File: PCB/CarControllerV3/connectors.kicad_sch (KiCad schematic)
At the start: 44 parts, among them J1 649012227222, J2 649012227222, Q2 AO3400A, U13 PC817X1NIP1B, U21 AP74700QW6-7

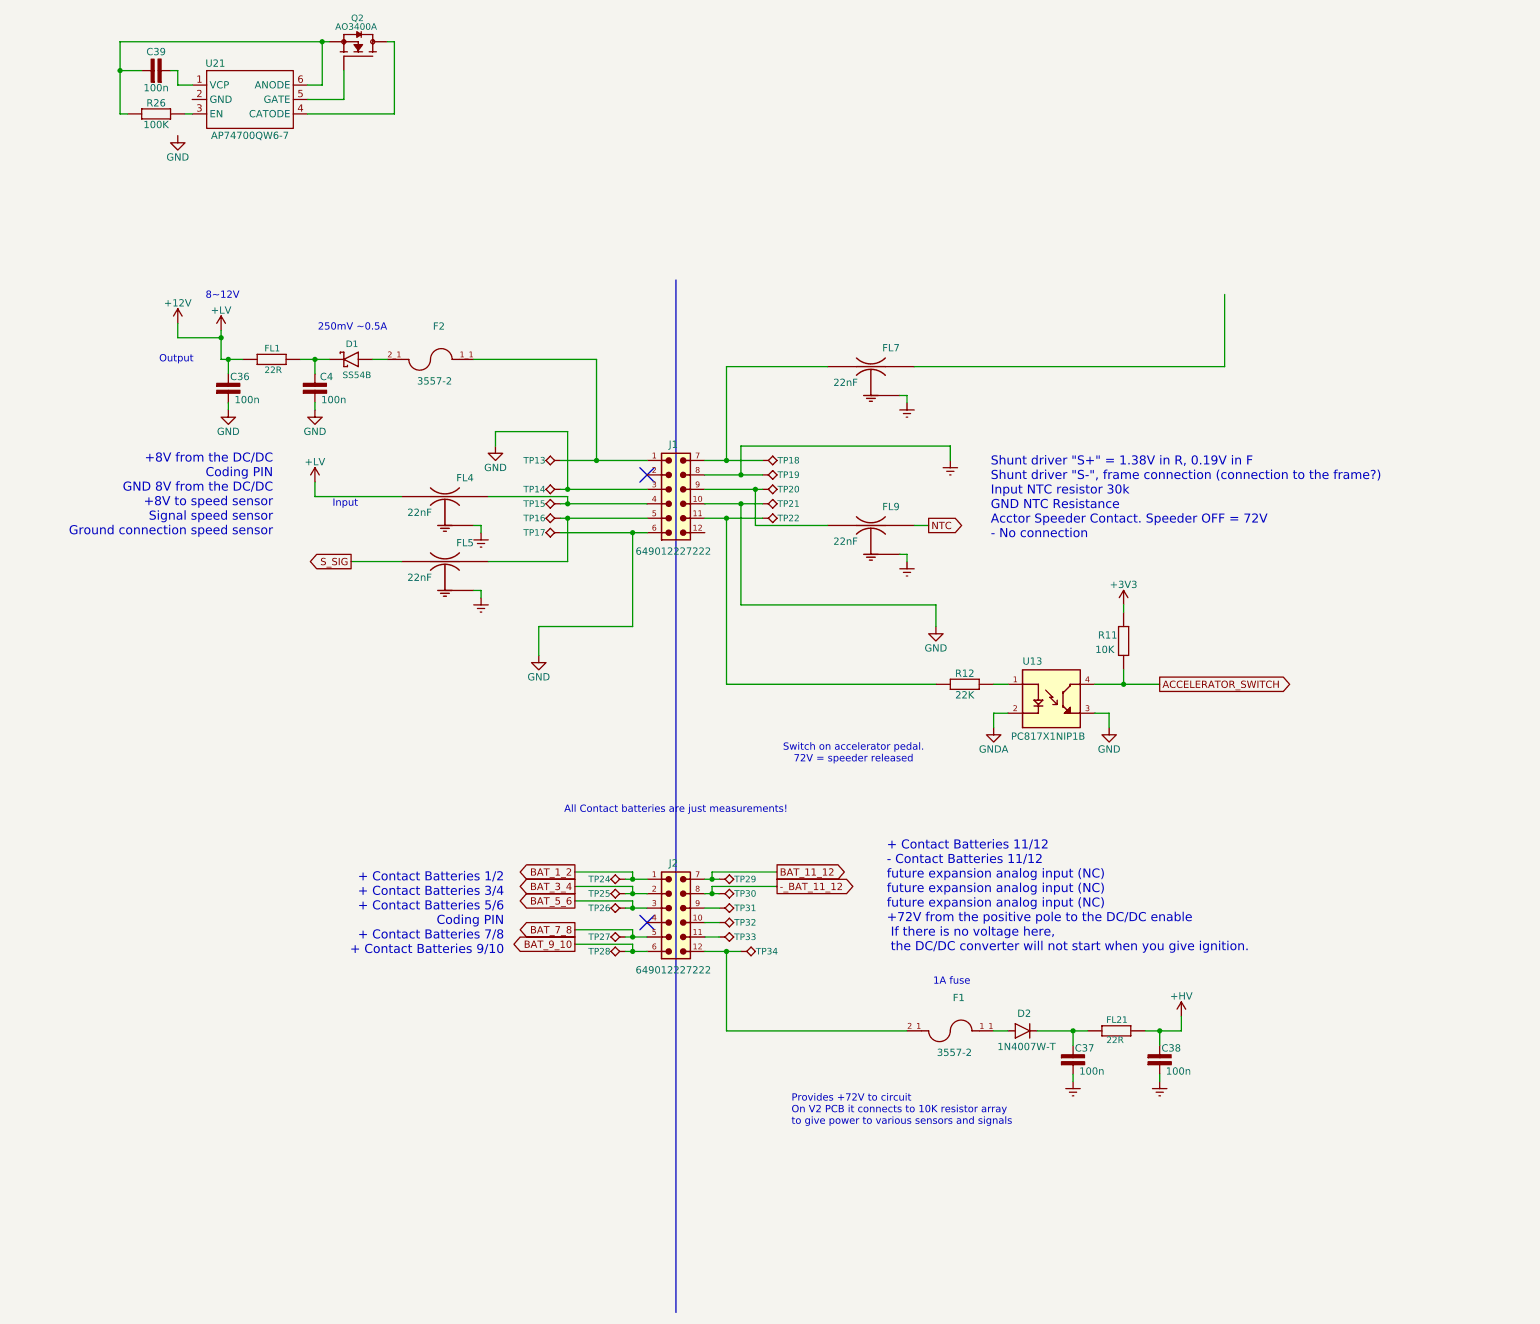
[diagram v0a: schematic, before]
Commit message: More work to PCB
- Rerouted bunch of connections
- Added alternative charge pump circuit
- Bunch of work on analog circuit
- Removed all the capacitor filter on the connectors in favor of filtering when nessesary.
- Placed canbus on JP5.2, JP5.3
- Disconnected various connections that needs to be decided if we should use.
- Added protection to various areas
- Added various todo notes everywhere..
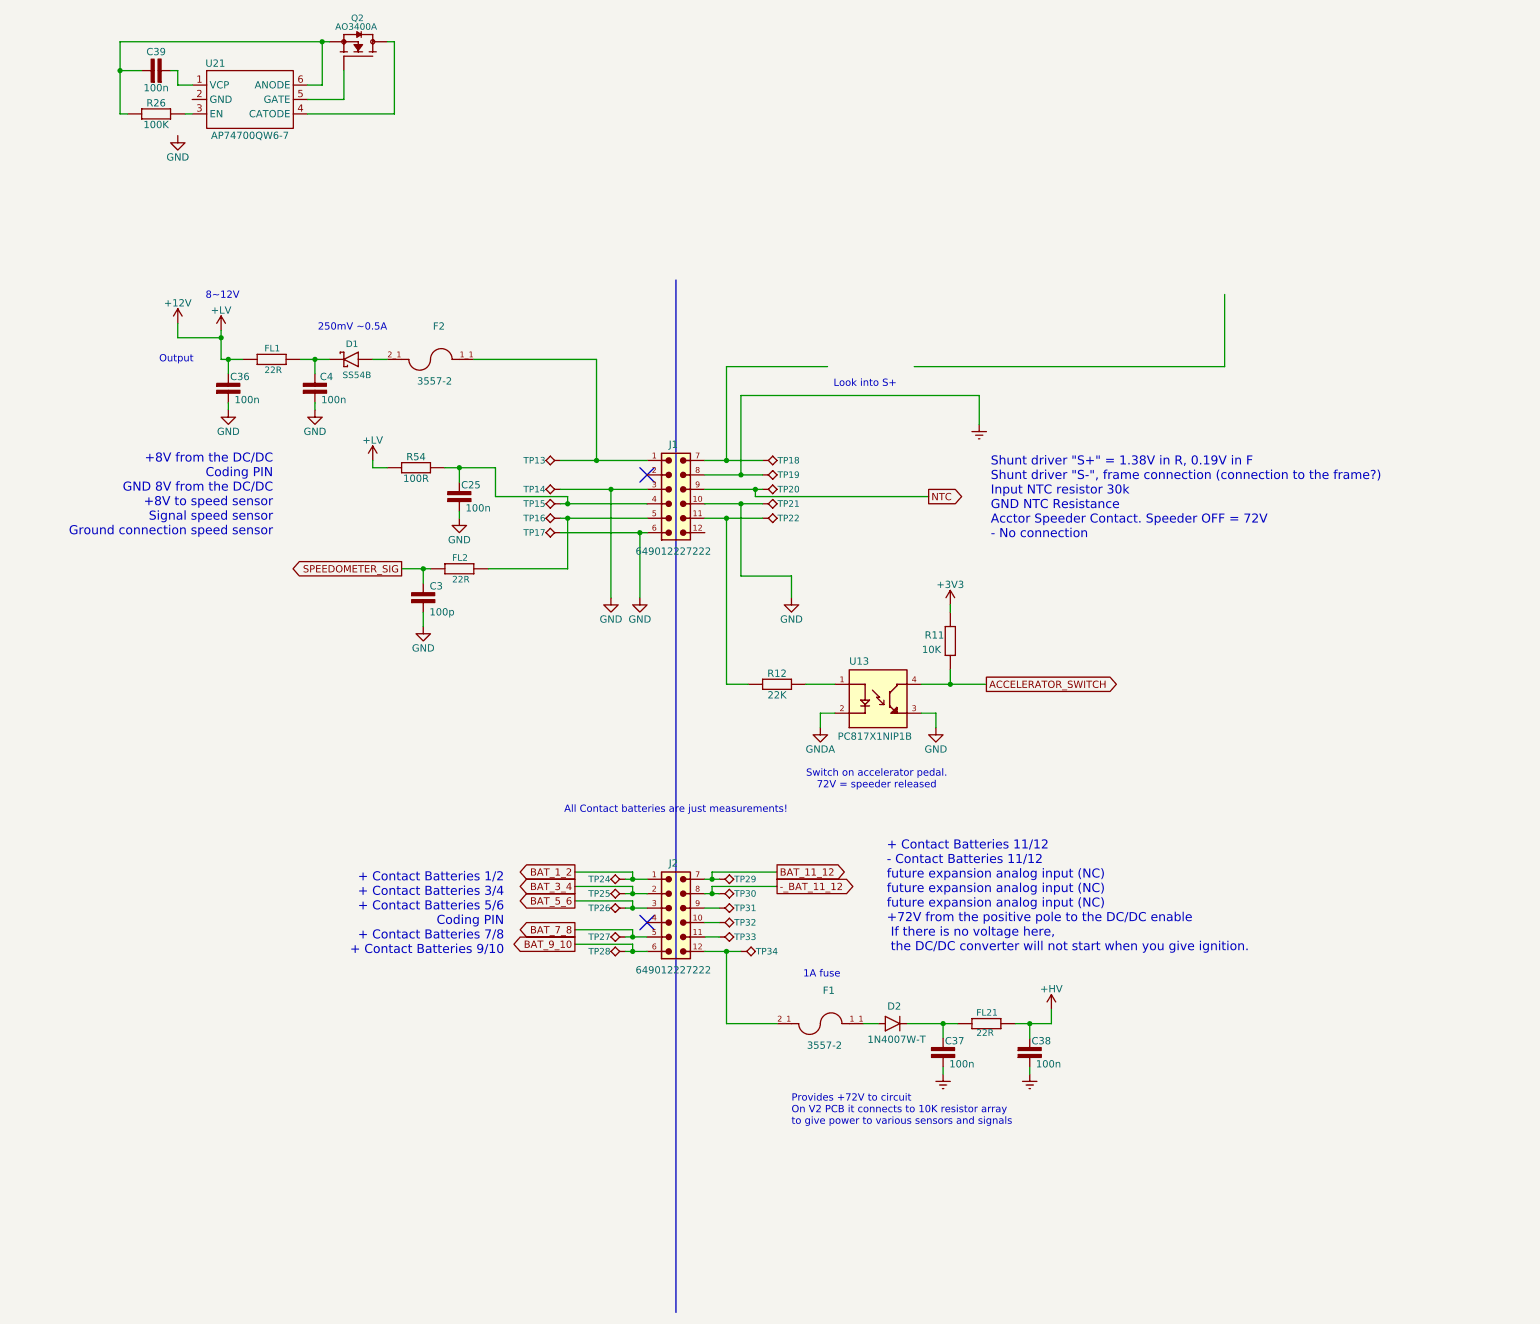
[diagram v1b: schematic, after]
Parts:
- removed FL4, FL5, FL7, FL9: 22nF, footprints:FIL_NFM21CC223R1H3D, symbol NFM21CC223R1H3D:NFM21CC223R1H3D
- added C25: 100n, footprints:CAPC1608X90, symbol CC0603:CC0603KRX7R9BB104
- added C3: 100p, footprints:, symbol CC0603:CC0603KRX7R9BB101
- added FL2: 22R, BLM18BA220SN1D:BLM18BA220SN1D-BEADC1608X95N, symbol BLM18BA220SN1D:BLM18BA220SN1D
- added R54: 100R, footprints:RC0603FR-RESC1608X60N, symbol RC0603FR:RC0603FR-07100R
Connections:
- net +12V: now also R54.2 (R2)
- net GND: now also C25.1 (C1), C3.1 (C1)
- net NTC: now also J1.9, TP20.TP
- net at J1.4, TP15.TP: now also C25.2 (C2), R54.1 (R1)
- net at J1.5, TP16.TP: now also FL2.1 (R1)
- new net SPEEDOMETER_SIG: C3.2 (C2), FL2.2 (R2)
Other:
- note added: "Look into S+"
- note removed: "Input"
- moved on the sheet: C37, C38, D2, F1, FL21, R11, R12, U13
